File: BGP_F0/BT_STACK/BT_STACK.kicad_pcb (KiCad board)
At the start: 2 copper layers, 24 x 26 mm, 19 parts, among them P1 CONN_01X05, P2 CONN_01X02, P3 CONN_01X04, U1 MC33178

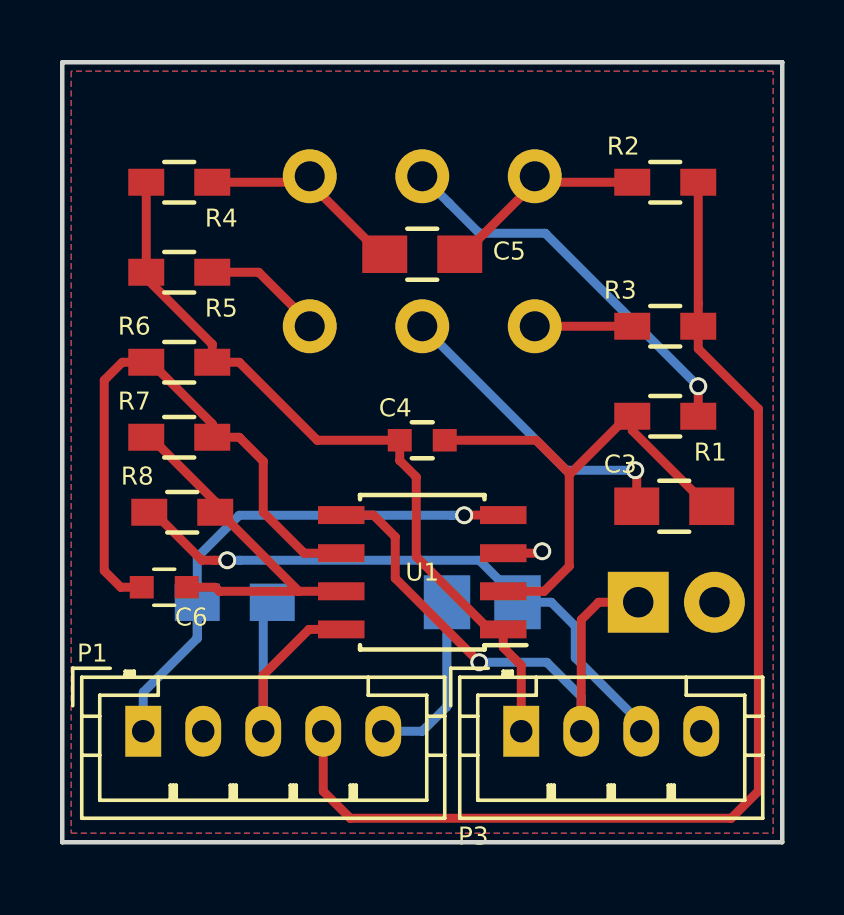
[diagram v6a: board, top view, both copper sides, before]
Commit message: Tone cap changed to female pin strip header for 0.047uF and 0.1uF
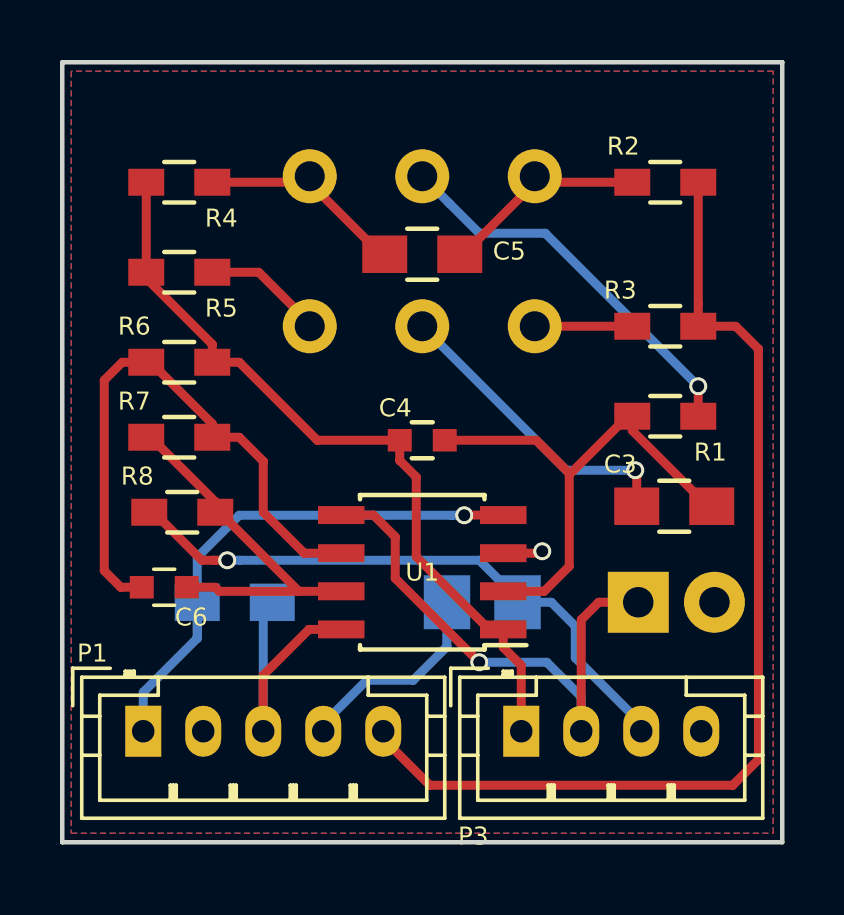
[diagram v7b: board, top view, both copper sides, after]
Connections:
- P1 pad 4: /IN -> /OUT
- P1 pad 5: /OUT -> /IN
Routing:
- net /IN: track 38.4 -> 34.6 mm
- net /OUT: track 5.94 -> 6.92 mm
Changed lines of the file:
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@@
     (thickness 1.6)
     (drawings 8)
-    (tracks 131)
+    (tracks 133)
     (zones 0)
     (modules 19)
@@
       (net 1 /V+))
     (pad 4 thru_hole oval (at 6 0) (size 1.2 1.7) (drill 0.75) (layers *.Cu *.Mask)
+      (net 4 /OUT))
+    (pad 5 thru_hole oval (at 8 0) (size 1.2 1.7) (drill 0.75) (layers *.Cu *.Mask)
       (net 11 /IN))
-    (pad 5 thru_hole oval (at 8 0) (size 1.2 1.7) (drill 0.75) (layers *.Cu *.Mask)
-      (net 4 /OUT))
     (model ${KISYS3DMOD}/Connectors_JST.3dshapes/JST_PH_B5B-PH-K_05x2.00mm_Straight.wrl
       (at (xyz 0 0 0))
@@
   (segment (start 159.3 91.3) (end 159.3 91.05) (width 0.3) (layer B.Cu) (net 3))
   (segment (start 159.3 91.05) (end 157.1 88.85) (width 0.3) (layer B.Cu) (net 3))
-  (segment (start 152 91.3) (end 152.82398 90.47602) (width 0.3) (layer B.Cu) (net 4))
-  (segment (start 152.82398 90.47602) (end 152.82398 87) (width 0.3) (layer B.Cu) (net 4))
-  (segment (start 150.7 91.3) (end 152 91.3) (width 0.3) (layer B.Cu) (net 4))
+  (segment (start 148.7 91.3) (end 148.7 91.05) (width 0.3) (layer B.Cu) (net 4))
+  (segment (start 151.7 89.6) (end 152.82398 88.47602) (width 0.3) (layer B.Cu) (net 4))
+  (segment (start 148.7 91.05) (end 150.15 89.6) (width 0.3) (layer B.Cu) (net 4))
+  (segment (start 150.15 89.6) (end 151.7 89.6) (width 0.3) (layer B.Cu) (net 4))
+  (segment (start 152.82398 88.47602) (end 152.82398 87) (width 0.3) (layer B.Cu) (net 4))
   (segment (start 159.1 82.6) (end 156.8 82.6) (width 0.3) (layer B.Cu) (net 5))
   (segment (start 156.8 82.6) (end 152 77.8) (width 0.3) (layer B.Cu) (net 5))
@@
   (segment (start 154.7 85.365) (end 155.935 85.365) (width 0.3) (layer F.Cu) (net 10))
   (via (at 156 85.3) (size 0.6) (drill 0.4) (layers F.Cu B.Cu) (net 10))
-  (segment (start 161.2 77.8) (end 161.2 78.55) (width 0.3) (layer F.Cu) (net 11))
-  (segment (start 161.2 78.55) (end 163.206001 80.556001) (width 0.3) (layer F.Cu) (net 11))
-  (segment (start 163.206001 80.556001) (end 163.206001 93.293999) (width 0.3) (layer F.Cu) (net 11))
-  (segment (start 163.206001 93.293999) (end 162.3 94.2) (width 0.3) (layer F.Cu) (net 11))
-  (segment (start 162.3 94.2) (end 149.6 94.2) (width 0.3) (layer F.Cu) (net 11))
-  (segment (start 149.6 94.2) (end 148.7 93.3) (width 0.3) (layer F.Cu) (net 11))
-  (segment (start 148.7 93.3) (end 148.7 91.3) (width 0.3) (layer F.Cu) (net 11))
+  (segment (start 163.206001 78.556001) (end 162.45 77.8) (width 0.3) (layer F.Cu) (net 11))
+  (segment (start 162.45 77.8) (end 161.2 77.8) (width 0.3) (layer F.Cu) (net 11))
+  (segment (start 162.35 93.1) (end 163.206001 92.243999) (width 0.3) (layer F.Cu) (net 11))
+  (segment (start 163.206001 92.243999) (end 163.206001 78.556001) (width 0.3) (layer F.Cu) (net 11))
+  (segment (start 152.25 93.1) (end 162.35 93.1) (width 0.3) (layer F.Cu) (net 11))
+  (segment (start 150.7 91.3) (end 150.7 91.55) (width 0.3) (layer F.Cu) (net 11))
+  (segment (start 150.7 91.55) (end 152.25 93.1) (width 0.3) (layer F.Cu) (net 11))
   (segment (start 161.2 77.8) (end 161.2 77.05) (width 0.3) (layer F.Cu) (net 11))
   (segment (start 161.2 77.05) (end 161.2 73) (width 0.3) (layer F.Cu) (net 11))

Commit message: Mid Buff
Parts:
- removed P2: CONN_01X02, Pin_Headers:Pin_Header_Straight_1x02
- added R9: 1.5MEG, Resistors_SMD:R_0603_HandSoldering, F.Cu at (160.0, 87.0)
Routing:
- net /Vref: track 1.33 -> 5.71 mm
- net /MID_R: track 18.3 -> 17.4 mm
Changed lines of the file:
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@@
     (thickness 1.6)
     (drawings 8)
-    (tracks 133)
+    (tracks 135)
     (zones 0)
     (modules 19)
@@
     )
   )
-  (module Pin_Headers:Pin_Header_Straight_1x02 (layer B.Cu)
-    (at 159.2 87 270)
-    (descr "Through hole pin header")
-    (tags "pin header")
-    (fp_text reference P2 (at -1.8 -3.3 360) (layer B.SilkS)
-      (effects (font (size 0.6 0.6) (thickness 0.15)) (justify mirror))
-    )
-    (fp_text value CONN_01X02 (at 0 3.1 270) (layer B.Fab) hide
-      (effects (font (size 0.6 0.6) (thickness 0.15)) (justify mirror))
-    )
-    (fp_line (start 1.27 -1.27) (end 1.27 -3.81) (layer B.SilkS) (width 0.15))
-    (fp_line (start 1.55 1.55) (end 1.55 0) (layer B.SilkS) (width 0.15))
-    (fp_line (start -1.75 1.75) (end -1.75 -4.3) (layer B.CrtYd) (width 0.05))
-    (fp_line (start 1.75 1.75) (end 1.75 -4.3) (layer B.CrtYd) (width 0.05))
-    (fp_line (start -1.75 1.75) (end 1.75 1.75) (layer B.CrtYd) (width 0.05))
-    (fp_line (start -1.75 -4.3) (end 1.75 -4.3) (layer B.CrtYd) (width 0.05))
-    (fp_line (start 1.27 -1.27) (end -1.27 -1.27) (layer B.SilkS) (width 0.15))
-    (fp_line (start -1.55 0) (end -1.55 1.55) (layer B.SilkS) (width 0.15))
-    (fp_line (start -1.55 1.55) (end 1.55 1.55) (layer B.SilkS) (width 0.15))
-    (fp_line (start -1.27 -1.27) (end -1.27 -3.81) (layer B.SilkS) (width 0.15))
-    (fp_line (start -1.27 -3.81) (end 1.27 -3.81) (layer B.SilkS) (width 0.15))
-    (pad 1 thru_hole rect (at 0 0 270) (size 2.032 2.032) (drill 1.016) (layers *.Cu *.Mask B.SilkS)
-      (net 12 /MID_R))
-    (pad 2 thru_hole oval (at 0 -2.54 270) (size 2.032 2.032) (drill 1.016) (layers *.Cu *.Mask B.SilkS)
-      (net 10 /Vref))
-    (model Pin_Headers.3dshapes/Pin_Header_Straight_1x02.wrl
-      (at (xyz 0 -0.05 0))
-      (scale (xyz 1 1 1))
-      (rotate (xyz 0 0 90))
-    )
-  )
   (module LIBS:Potentiometer_Alpha_Double_Vertical_Dual_Shaft (layer B.Cu)
     (at 148.25 72.8 90)
@@
       (net 17 "Net-(C6-Pad1)"))
     (model Capacitors_SMD.3dshapes/C_0603.wrl
+      (at (xyz 0 0 0))
+      (scale (xyz 1 1 1))
+      (rotate (xyz 0 0 0))
+    )
+  )
+  (module Resistors_SMD:R_0603_HandSoldering (layer F.Cu)
+    (at 160 87)
+    (descr "Resistor SMD 0603, hand soldering")
+    (tags "resistor 0603")
+    (attr smd)
+    (fp_text reference R9 (at -1.5 -1) (layer F.SilkS)
+      (effects (font (size 0.6 0.6) (thickness 0.15)))
+    )
+    (fp_text value 1.5MEG (at 0 1.55) (layer F.Fab) hide
+      (effects (font (size 0.6 0.6) (thickness 0.15)))
+    )
+    (fp_text user %R (at 0 0) (layer F.Fab) hide
+      (effects (font (size 0.4 0.4) (thickness 0.075)))
+    )
+    (fp_line (start -0.8 0.4) (end -0.8 -0.4) (layer F.Fab) (width 0.1))
+    (fp_line (start 0.8 0.4) (end -0.8 0.4) (layer F.Fab) (width 0.1))
+    (fp_line (start 0.8 -0.4) (end 0.8 0.4) (layer F.Fab) (width 0.1))
+    (fp_line (start -0.8 -0.4) (end 0.8 -0.4) (layer F.Fab) (width 0.1))
+    (fp_line (start 0.5 0.68) (end -0.5 0.68) (layer F.SilkS) (width 0.12))
+    (fp_line (start -0.5 -0.68) (end 0.5 -0.68) (layer F.SilkS) (width 0.12))
+    (fp_line (start -1.96 -0.7) (end 1.95 -0.7) (layer F.CrtYd) (width 0.05))
+    (fp_line (start -1.96 -0.7) (end -1.96 0.7) (layer F.CrtYd) (width 0.05))
+    (fp_line (start 1.95 0.7) (end 1.95 -0.7) (layer F.CrtYd) (width 0.05))
+    (fp_line (start 1.95 0.7) (end -1.96 0.7) (layer F.CrtYd) (width 0.05))
+    (pad 1 smd rect (at -1.1 0) (size 1.2 0.9) (layers F.Cu F.Paste F.Mask)
+      (net 12 /MID_R))
+    (pad 2 smd rect (at 1.1 0) (size 1.2 0.9) (layers F.Cu F.Paste F.Mask)
+      (net 10 /Vref))
+    (model ${KISYS3DMOD}/Resistors_SMD.3dshapes/R_0603.wrl
       (at (xyz 0 0 0))
       (scale (xyz 1 1 1))
@@
   (segment (start 148.15 73) (end 148.35 72.8) (width 0.3) (layer F.Cu) (net 9))
   (segment (start 150.75 75.2) (end 150.75 75.4) (width 0.3) (layer F.Cu) (net 9))
+  (segment (start 161.1 87) (end 161.3 87.2) (width 0.3) (layer F.Cu) (net 10))
+  (segment (start 161.3 87.2) (end 161.3 91.3) (width 0.3) (layer F.Cu) (net 10))
   (segment (start 155.935 85.365) (end 156 85.3) (width 0.3) (layer F.Cu) (net 10))
   (segment (start 154.7 85.365) (end 155.935 85.365) (width 0.3) (layer F.Cu) (net 10))
@@
   (segment (start 161.2 77.8) (end 161.2 77.05) (width 0.3) (layer F.Cu) (net 11))
   (segment (start 161.2 77.05) (end 161.2 73) (width 0.3) (layer F.Cu) (net 11))
+  (segment (start 158.9 87) (end 158.9 87.75) (width 0.3) (layer F.Cu) (net 12))
+  (segment (start 158.9 87.75) (end 157.3 89.35) (width 0.3) (layer F.Cu) (net 12))
+  (segment (start 157.3 89.35) (end 157.3 91.3) (width 0.3) (layer F.Cu) (net 12))
   (segment (start 153.9 89) (end 156.15 89) (width 0.3) (layer B.Cu) (net 12))
   (segment (start 156.15 89) (end 157.3 90.15) (width 0.3) (layer B.Cu) (net 12))
@@
   (segment (start 149.3 84.095) (end 150.375 84.095) (width 0.3) (layer F.Cu) (net 12))
   (segment (start 150.375 84.095) (end 151.1 84.82) (width 0.3) (layer F.Cu) (net 12))
-  (segment (start 157.3 91.3) (end 157.3 87.584) (width 0.3) (layer F.Cu) (net 12))
-  (segment (start 157.3 87.584) (end 157.884 87) (width 0.3) (layer F.Cu) (net 12))
-  (segment (start 157.884 87) (end 159.2 87) (width 0.3) (layer F.Cu) (net 12))
   (segment (start 161.2 79.8) (end 156.1 74.7) (width 0.3) (layer B.Cu) (net 13))
   (segment (start 156.1 74.7) (end 153.9 74.7) (width 0.3) (layer B.Cu) (net 13))
